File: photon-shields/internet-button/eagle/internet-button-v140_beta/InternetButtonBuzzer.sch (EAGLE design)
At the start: 43 parts

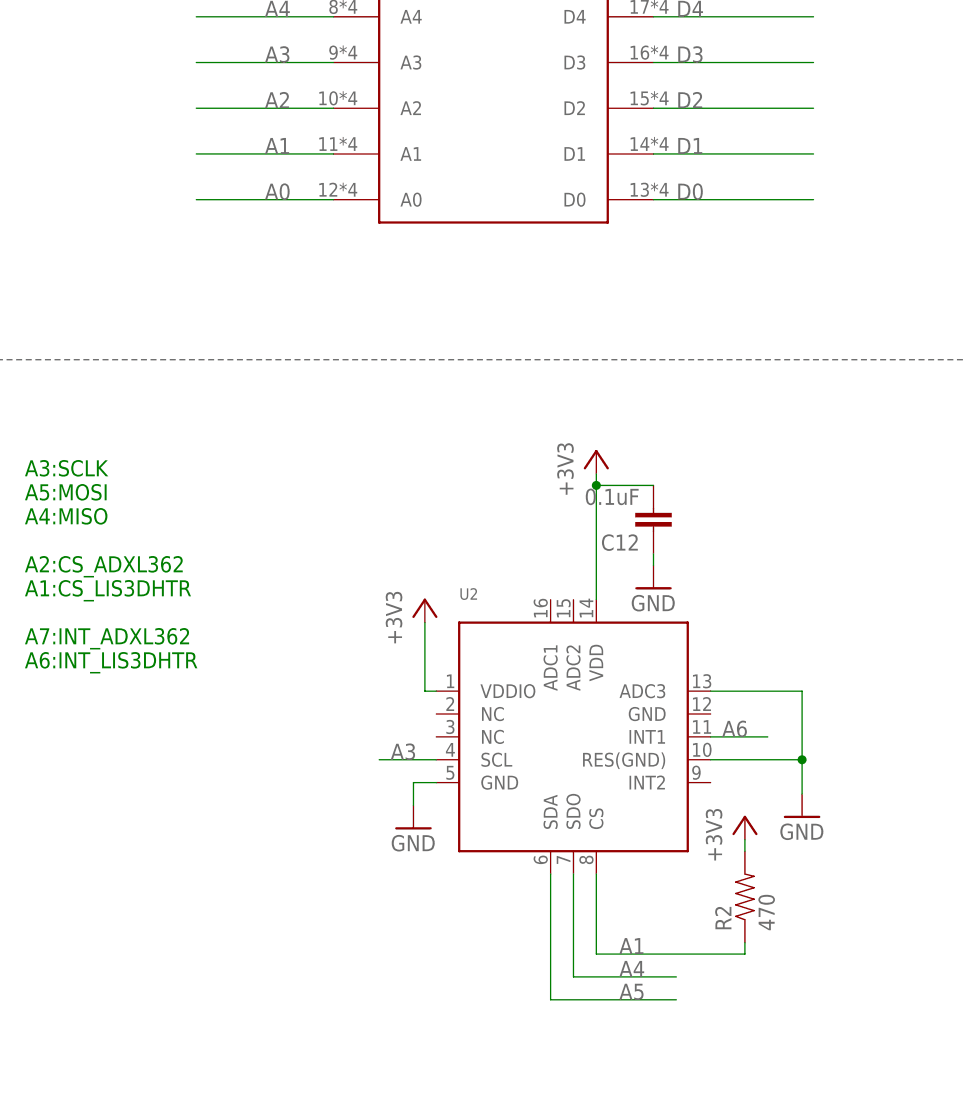
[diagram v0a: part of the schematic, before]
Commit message: update the design file since i catch some error from last version
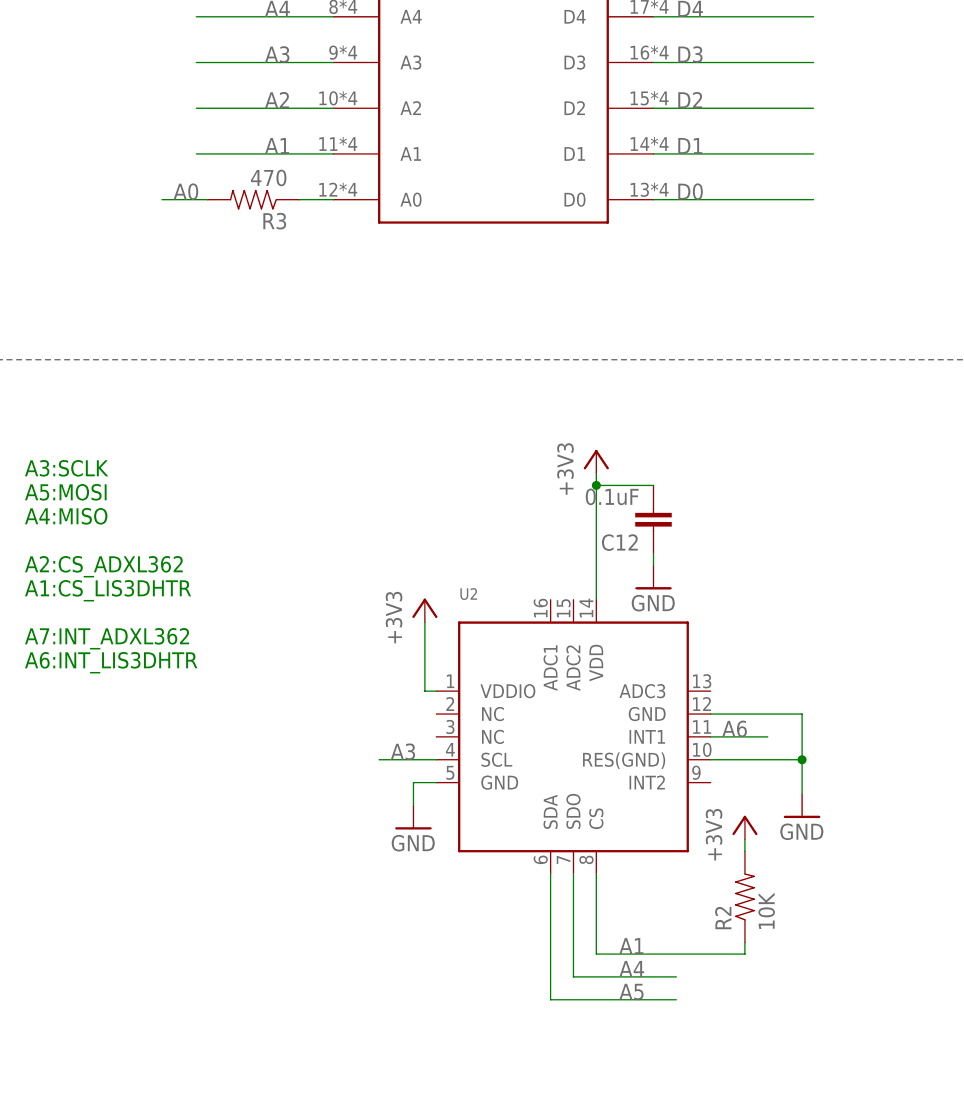
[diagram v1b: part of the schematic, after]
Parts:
- added R3: 470, SparkFun-Resistors:470OHM1/10W1%(0603)
- R2: value 470 -> 10K
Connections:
- removed net GND@1: U2.GND@1
- new net N$4: R3.1, U$7.A0
- net A0: now also R3.2; no longer U$7.A0
- net GND: now also U2.GND@1, U2.GND@2; no longer U2.ADC3
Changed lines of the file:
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@@
 <setting verticaltext="up"/>
 </settings>
-<grid distance="10" unitdist="mil" unit="mil" style="lines" multiple="1" display="no" altdistance="0.01" altunitdist="inch" altunit="inch"/>
+<grid distance="50" unitdist="mil" unit="mil" style="lines" multiple="1" display="no" altdistance="0.01" altunitdist="inch" altunit="inch"/>
 <layers>
 <layer number="1" name="Top" color="4" fill="1" visible="no" active="no"/>
@@
 <part name="+3V5" library="supply1" deviceset="+3V3" device=""/>
 <part name="C12" library="SparkFun-Passives" deviceset="CAP" device="0603-CAP" value="0.1uF"/>
-<part name="R2" library="SparkFun-Resistors" deviceset="470OHM1/10W1%(0603)" device="" value="470"/>
+<part name="R2" library="SparkFun-Resistors" deviceset="470OHM1/10W1%(0603)" device="" value="10K"/>
 <part name="+3V6" library="supply1" deviceset="+3V3" device=""/>
 <part name="GND21" library="SparkFun-Aesthetics" deviceset="GND" device=""/>
@@
 <part name="C14" library="SparkFun-Passives" deviceset="CAP" device="0603-CAP" value="10uF"/>
 <part name="GND24" library="SparkFun-Aesthetics" deviceset="GND" device=""/>
+<part name="R3" library="SparkFun-Resistors" deviceset="470OHM1/10W1%(0603)" device="" value="470"/>
 </parts>
 <sheets>
@@
 <instance part="C14" gate="G$1" x="164.338" y="123.19"/>
 <instance part="GND24" gate="1" x="164.338" y="115.57"/>
+<instance part="R3" gate="G$1" x="213.36" y="151.13" rot="R180"/>
 </instances>
 <busses>
@@
 </segment>
 <segment>
-<pinref part="U2" gate="G$1" pin="ADC3"/>
 <pinref part="GND21" gate="1" pin="GND"/>
-<wire x1="264.16" y1="96.52" x2="274.32" y2="96.52" width="0.1524" layer="91"/>
-<wire x1="274.32" y1="96.52" x2="274.32" y2="88.9" width="0.1524" layer="91"/>
 <pinref part="U2" gate="G$1" pin="RES(GND)"/>
 <wire x1="274.32" y1="88.9" x2="274.32" y2="85.09" width="0.1524" layer="91"/>
 <wire x1="264.16" y1="88.9" x2="274.32" y2="88.9" width="0.1524" layer="91"/>
+<pinref part="U2" gate="G$1" pin="GND@2"/>
+<wire x1="264.16" y1="93.98" x2="274.32" y2="93.98" width="0.1524" layer="91"/>
+<wire x1="274.32" y1="93.98" x2="274.32" y2="88.9" width="0.1524" layer="91"/>
 <junction x="274.32" y="88.9"/>
 </segment>
@@
 <pinref part="GND24" gate="1" pin="GND"/>
 <wire x1="164.338" y1="120.65" x2="164.338" y2="118.11" width="0.1524" layer="91"/>
+</segment>
+<segment>
+<pinref part="U2" gate="G$1" pin="GND@1"/>
+<pinref part="GND23" gate="1" pin="GND"/>
+<wire x1="233.68" y1="86.36" x2="231.14" y2="86.36" width="0.1524" layer="91"/>
+<wire x1="231.14" y1="86.36" x2="231.14" y2="83.82" width="0.1524" layer="91"/>
 </segment>
 </net>
@@
 </net>
 <net name="A0" class="0">
-<segment>
-<label x="214.63" y="151.13" size="1.778" layer="95"/>
-<wire x1="222.25" y1="151.13" x2="207.01" y2="151.13" width="0.1524" layer="91"/>
-<pinref part="U$7" gate="G$1" pin="A0"/>
-</segment>
 <segment>
 <wire x1="146.05" y1="130.81" x2="146.05" y2="128.27" width="0.1524" layer="91"/>
@@
 <junction x="158.75" y="130.81"/>
 </segment>
+<segment>
+<pinref part="R3" gate="G$1" pin="2"/>
+<wire x1="208.28" y1="151.13" x2="203.2" y2="151.13" width="0.1524" layer="91"/>
+<label x="204.47" y="151.13" size="1.778" layer="95"/>
+</segment>
 </net>
 <net name="N$14" class="0">
@@
 </segment>
 </net>
-<net name="GND@1" class="0">
-<segment>
-<pinref part="U2" gate="G$1" pin="GND@1"/>
-<pinref part="GND23" gate="1" pin="GND"/>
-<wire x1="233.68" y1="86.36" x2="231.14" y2="86.36" width="0.1524" layer="91"/>
-<wire x1="231.14" y1="86.36" x2="231.14" y2="83.82" width="0.1524" layer="91"/>
-</segment>
-</net>
+<net name="N$4" class="0">
+<segment>
+<pinref part="U$7" gate="G$1" pin="A0"/>
+<pinref part="R3" gate="G$1" pin="1"/>
+<wire x1="222.25" y1="151.13" x2="218.44" y2="151.13" width="0.1524" layer="91"/>
+</segment>
+</net>

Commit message: update the pcb file for internet button
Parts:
- removed 12: M01PTH, SparkFun-Connectors:M01PTH
- removed C14: 10uF, SparkFun-Passives:CAP0603-CAP
- removed R3: 470, SparkFun-Resistors:470OHM1/10W1%(0603)
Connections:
- removed net A0: C13.1, C14.1, R3.2, U1.VDDIO, U1.VS
- net +3V3: now also C13.1, U1.VDDIO, U1.VS
- net D6: now also U$5.3
- net GND: now also U$5.1; no longer C14.2
- net N$4: no longer R3.1
- net N$5: no longer 12.1
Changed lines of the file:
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@@
 <setting verticaltext="up"/>
 </settings>
-<grid distance="50" unitdist="mil" unit="mil" style="lines" multiple="1" display="no" altdistance="0.01" altunitdist="inch" altunit="inch"/>
+<grid distance="0.1" unitdist="inch" unit="inch" style="lines" multiple="1" display="no" altdistance="0.01" altunitdist="inch" altunit="inch"/>
 <layers>
 <layer number="1" name="Top" color="4" fill="1" visible="no" active="no"/>
@@
 <part name="3.3V" library="SparkFun-Connectors" deviceset="M03" device="LOCK_NO_SILK"/>
 <part name="GND" library="SparkFun-Connectors" deviceset="M03" device="LOCK_NO_SILK"/>
-<part name="12" library="SparkFun-Connectors" deviceset="M01" device="PTH"/>
 <part name="SG1" library="SparkFun-Electromechanical" deviceset="BUZZER" device="SMD2"/>
 <part name="JP2" library="SparkFun-Connectors" deviceset="M02" device="PTH"/>
@@
 <part name="GND22" library="SparkFun-Aesthetics" deviceset="GND" device=""/>
 <part name="GND23" library="SparkFun-Aesthetics" deviceset="GND" device=""/>
-<part name="C14" library="SparkFun-Passives" deviceset="CAP" device="0603-CAP" value="10uF"/>
-<part name="GND24" library="SparkFun-Aesthetics" deviceset="GND" device=""/>
-<part name="R3" library="SparkFun-Resistors" deviceset="470OHM1/10W1%(0603)" device="" value="470"/>
+<part name="+3V2" library="supply1" deviceset="+3V3" device=""/>
 </parts>
 <sheets>
@@
 <instance part="3.3V" gate="G$1" x="281.94" y="243.84" rot="MR0"/>
 <instance part="GND" gate="G$1" x="256.54" y="243.84" rot="R180"/>
-<instance part="12" gate="G$1" x="31.75" y="36.83"/>
 <instance part="SG1" gate="G$1" x="132.08" y="251.46" rot="MR270"/>
 <instance part="JP2" gate="G$1" x="232.41" y="246.38" rot="R180"/>
@@
 <instance part="GND22" gate="1" x="257.81" y="107.95"/>
 <instance part="GND23" gate="1" x="231.14" y="81.28"/>
-<instance part="C14" gate="G$1" x="164.338" y="123.19"/>
-<instance part="GND24" gate="1" x="164.338" y="115.57"/>
-<instance part="R3" gate="G$1" x="213.36" y="151.13" rot="R180"/>
+<instance part="+3V2" gate="G$1" x="158.75" y="137.16"/>
 </instances>
 <busses>
@@
 <wire x1="124.46" y1="33.02" x2="124.46" y2="27.94" width="0.1524" layer="91"/>
 <junction x="124.46" y="33.02"/>
+<pinref part="U$5" gate="G$1" pin="1"/>
+<wire x1="132.08" y1="48.26" x2="132.08" y2="45.72" width="0.1524" layer="91"/>
+<junction x="132.08" y="45.72"/>
 </segment>
 <segment>
@@
 </segment>
 <segment>
-<pinref part="C14" gate="G$1" pin="2"/>
-<pinref part="GND24" gate="1" pin="GND"/>
-<wire x1="164.338" y1="120.65" x2="164.338" y2="118.11" width="0.1524" layer="91"/>
-</segment>
-<segment>
 <pinref part="U2" gate="G$1" pin="GND@1"/>
 <pinref part="GND23" gate="1" pin="GND"/>
@@
 </segment>
 </net>
-<net name="A0" class="0">
-<segment>
-<wire x1="146.05" y1="130.81" x2="146.05" y2="128.27" width="0.1524" layer="91"/>
-<pinref part="U1" gate="G$1" pin="VS"/>
-<wire x1="146.05" y1="128.27" x2="144.78" y2="128.27" width="0.1524" layer="91"/>
-<pinref part="C13" gate="G$1" pin="1"/>
-<wire x1="146.05" y1="130.81" x2="158.75" y2="130.81" width="0.1524" layer="91"/>
-<wire x1="158.75" y1="130.81" x2="158.75" y2="128.27" width="0.1524" layer="91"/>
-<pinref part="U1" gate="G$1" pin="VDDIO"/>
-<wire x1="144.78" y1="130.81" x2="146.05" y2="130.81" width="0.1524" layer="91"/>
-<junction x="146.05" y="130.81"/>
-<label x="155.448" y="131.064" size="1.778" layer="95"/>
-<pinref part="C14" gate="G$1" pin="1"/>
-<wire x1="164.338" y1="128.27" x2="164.338" y2="130.81" width="0.1524" layer="91"/>
-<wire x1="164.338" y1="130.81" x2="158.75" y2="130.81" width="0.1524" layer="91"/>
-<junction x="158.75" y="130.81"/>
-</segment>
-<segment>
-<pinref part="R3" gate="G$1" pin="2"/>
-<wire x1="208.28" y1="151.13" x2="203.2" y2="151.13" width="0.1524" layer="91"/>
-<label x="204.47" y="151.13" size="1.778" layer="95"/>
-</segment>
-</net>
 <net name="N$14" class="0">
 <segment>
@@
 <wire x1="142.24" y1="45.72" x2="148.59" y2="45.72" width="0.1524" layer="91"/>
 <label x="144.78" y="45.72" size="1.778" layer="95"/>
+<pinref part="U$5" gate="G$1" pin="3"/>
+<wire x1="142.24" y1="48.26" x2="142.24" y2="45.72" width="0.1524" layer="91"/>
+<junction x="142.24" y="45.72"/>
 </segment>
 </net>
@@
 <net name="N$5" class="0">
 <segment>
-<pinref part="12" gate="G$1" pin="1"/>
 <pinref part="11" gate="G$1" pin="DOUT"/>
 <wire x1="39.37" y1="36.83" x2="52.07" y2="36.83" width="0.1524" layer="91"/>
 <wire x1="39.37" y1="36.83" x2="39.37" y2="26.67" width="0.1524" layer="91"/>
-<junction x="39.37" y="36.83"/>
 <wire x1="39.37" y1="26.67" x2="74.93" y2="26.67" width="0.1524" layer="91"/>
 <pinref part="12TH" gate="G$1" pin="DIN"/>
@@
 <wire x1="232.41" y1="96.52" x2="233.68" y2="96.52" width="0.1524" layer="91"/>
 </segment>
+<segment>
+<wire x1="146.05" y1="130.81" x2="146.05" y2="128.27" width="0.1524" layer="91"/>
+<pinref part="U1" gate="G$1" pin="VS"/>
+<wire x1="146.05" y1="128.27" x2="144.78" y2="128.27" width="0.1524" layer="91"/>
+<pinref part="U1" gate="G$1" pin="VDDIO"/>
+<wire x1="144.78" y1="130.81" x2="146.05" y2="130.81" width="0.1524" layer="91"/>
+<pinref part="C13" gate="G$1" pin="1"/>
+<wire x1="158.75" y1="128.27" x2="158.75" y2="130.81" width="0.1524" layer="91"/>
+<wire x1="158.75" y1="130.81" x2="146.05" y2="130.81" width="0.1524" layer="91"/>
+<junction x="146.05" y="130.81"/>
+<pinref part="+3V2" gate="G$1" pin="+3V3"/>
+<wire x1="158.75" y1="134.62" x2="158.75" y2="130.81" width="0.1524" layer="91"/>
+<junction x="158.75" y="130.81"/>
+</segment>
 </net>
 <net name="N$3" class="0">
@@
 <segment>
 <pinref part="U$7" gate="G$1" pin="A0"/>
-<pinref part="R3" gate="G$1" pin="1"/>
 <wire x1="222.25" y1="151.13" x2="218.44" y2="151.13" width="0.1524" layer="91"/>
 </segment>
